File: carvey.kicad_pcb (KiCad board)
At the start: 2 copper layers, 48.2 x 14.7 mm, 2 parts, among them J1 Conn_01x04, SW1 SW_Push_Dual

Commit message: Added holes, carved it with Carvey itself, without autoleveling
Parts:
- added REF**: M2.5_HOLE, adamgreig/agg-kicad/agg.pretty:M2.5_HOLE, F.Cu at (140.8, 100.2)
- added REF**: M2.5_HOLE, adamgreig/agg-kicad/agg.pretty:M2.5_HOLE, F.Cu at (130.9, 100.2)
- added REF**: M2.5_HOLE, adamgreig/agg-kicad/agg.pretty:M2.5_HOLE, F.Cu at (140.8, 90.5)
- added REF**: M2.5_HOLE, adamgreig/agg-kicad/agg.pretty:M2.5_HOLE, F.Cu at (130.9, 90.4)
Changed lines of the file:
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@@
   (tracks 16)
   (zones 0)
-  (modules 2)
+  (modules 6)
   (nets 3)
 )
@@
   (tracks 16)
   (zones 0)
-  (modules 2)
+  (modules 6)
   (nets 3)
 )
@@
 )
 (setup
-  (last_trace_width 1)
+  (last_trace_width 0.25)
   (user_trace_width 1)
   (user_trace_width 2)
@@
   (mod_text_size 1 1)
   (mod_text_width 0.15)
-  (pad_size 1.524 1.524)
-  (pad_drill 0.762)
+  (pad_size 2 2)
+  (pad_drill 2)
   (pad_to_mask_clearance 0.2)
   (aux_axis_origin 127.05 102.65)
@@
     (viasonmask false)
     (mode 1)
-    (useauxorigin false)
+    (useauxorigin true)
     (hpglpennumber 1)
     (hpglpenspeed 20)
@@
     (drillshape 0)
     (scaleselection 1)
-    (outputdirectory homefab))
+    (outputdirectory homefab/))
 )
 (net 0 "")
@@
   (add_net "Net-(J1-Pad2)")
 )
+  (module adamgreig/agg-kicad/agg.pretty:M2.5_HOLE (layer F.Cu)
+    (at 140.85 100.2)
+    (fp_text reference REF** (at 0 -2.5) (layer F.Fab) hide
+      (effects (font (size 1 1) (thickness 0.15)))
+    )
+    (fp_text value M2.5_HOLE (at 0 2.5) (layer F.Fab) hide
+      (effects (font (size 1 1) (thickness 0.15)))
+    )
+    (fp_line (start -1.8 -1.8) (end 1.8 -1.8) (layer F.CrtYd) (width 0.01))
+    (fp_line (start 1.8 -1.8) (end 1.8 1.8) (layer F.CrtYd) (width 0.01))
+    (fp_line (start 1.8 1.8) (end -1.8 1.8) (layer F.CrtYd) (width 0.01))
+    (fp_line (start -1.8 1.8) (end -1.8 -1.8) (layer F.CrtYd) (width 0.01))
+    (pad "" np_thru_hole circle (at 0 0) (size 2 2) (drill 2) (layers *.Cu F.Mask))
+  )
+  (module adamgreig/agg-kicad/agg.pretty:M2.5_HOLE (layer F.Cu)
+    (at 130.9 100.2)
+    (fp_text reference REF** (at 0 -2.5) (layer F.Fab) hide
+      (effects (font (size 1 1) (thickness 0.15)))
+    )
+    (fp_text value M2.5_HOLE (at 0 2.5) (layer F.Fab) hide
+      (effects (font (size 1 1) (thickness 0.15)))
+    )
+    (fp_line (start -1.8 -1.8) (end 1.8 -1.8) (layer F.CrtYd) (width 0.01))
+    (fp_line (start 1.8 -1.8) (end 1.8 1.8) (layer F.CrtYd) (width 0.01))
+    (fp_line (start 1.8 1.8) (end -1.8 1.8) (layer F.CrtYd) (width 0.01))
+    (fp_line (start -1.8 1.8) (end -1.8 -1.8) (layer F.CrtYd) (width 0.01))
+    (pad "" np_thru_hole circle (at 0 0) (size 2 2) (drill 2) (layers *.Cu F.Mask))
+  )
+  (module adamgreig/agg-kicad/agg.pretty:M2.5_HOLE (layer F.Cu)
+    (at 140.85 90.45)
+    (fp_text reference REF** (at 0 -2.5) (layer F.Fab) hide
+      (effects (font (size 1 1) (thickness 0.15)))
+    )
+    (fp_text value M2.5_HOLE (at 0 2.5) (layer F.Fab) hide
+      (effects (font (size 1 1) (thickness 0.15)))
+    )
+    (fp_line (start -1.8 -1.8) (end 1.8 -1.8) (layer F.CrtYd) (width 0.01))
+    (fp_line (start 1.8 -1.8) (end 1.8 1.8) (layer F.CrtYd) (width 0.01))
+    (fp_line (start 1.8 1.8) (end -1.8 1.8) (layer F.CrtYd) (width 0.01))
+    (fp_line (start -1.8 1.8) (end -1.8 -1.8) (layer F.CrtYd) (width 0.01))
+    (pad "" np_thru_hole circle (at 0 0) (size 2 2) (drill 2) (layers *.Cu F.Mask))
+  )
+  (module adamgreig/agg-kicad/agg.pretty:M2.5_HOLE (layer F.Cu)
+    (at 130.925 90.4)
+    (fp_text reference REF** (at 0 -2.5) (layer F.Fab) hide
+      (effects (font (size 1 1) (thickness 0.15)))
+    )
+    (fp_text value M2.5_HOLE (at 0 2.5) (layer F.Fab) hide
+      (effects (font (size 1 1) (thickness 0.15)))
+    )
+    (fp_line (start -1.8 -1.8) (end 1.8 -1.8) (layer F.CrtYd) (width 0.01))
+    (fp_line (start 1.8 -1.8) (end 1.8 1.8) (layer F.CrtYd) (width 0.01))
+    (fp_line (start 1.8 1.8) (end -1.8 1.8) (layer F.CrtYd) (width 0.01))
+    (fp_line (start -1.8 1.8) (end -1.8 -1.8) (layer F.CrtYd) (width 0.01))
+    (pad "" np_thru_hole circle (at 0 0) (size 2 2) (drill 2) (layers *.Cu F.Mask))
+  )
   (module KiCad/Connectors_JST.pretty:JST_PH_S4B-PH-SM4-TB_04x2.00mm_Angled (layer F.Cu)
     (at 153.5 95.025 90)

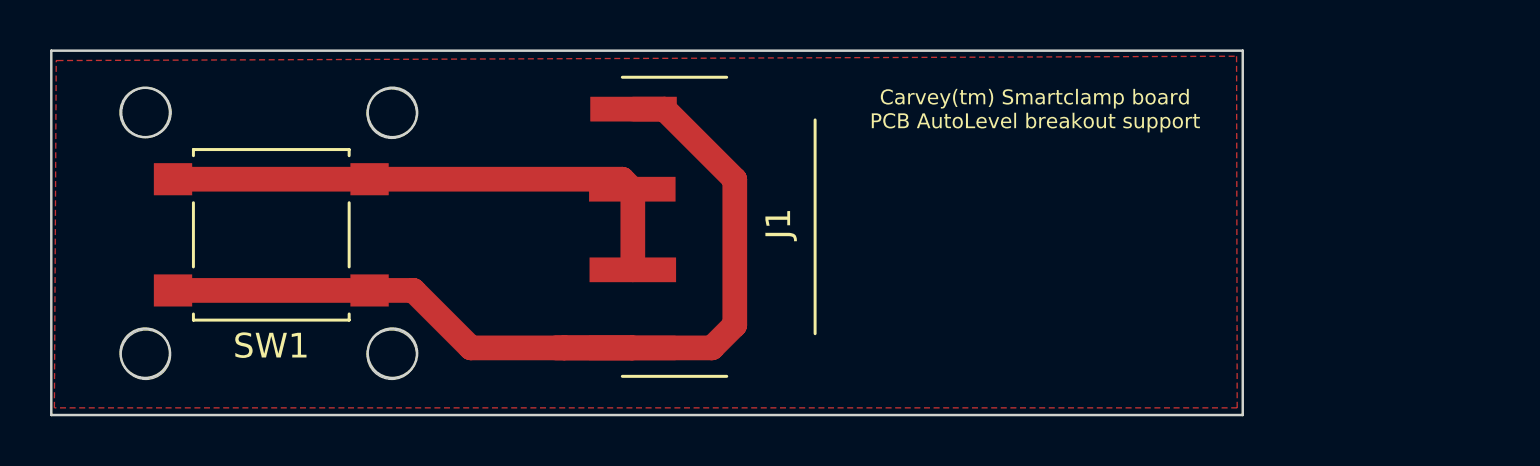
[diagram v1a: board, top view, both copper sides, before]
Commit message: Track too near pad
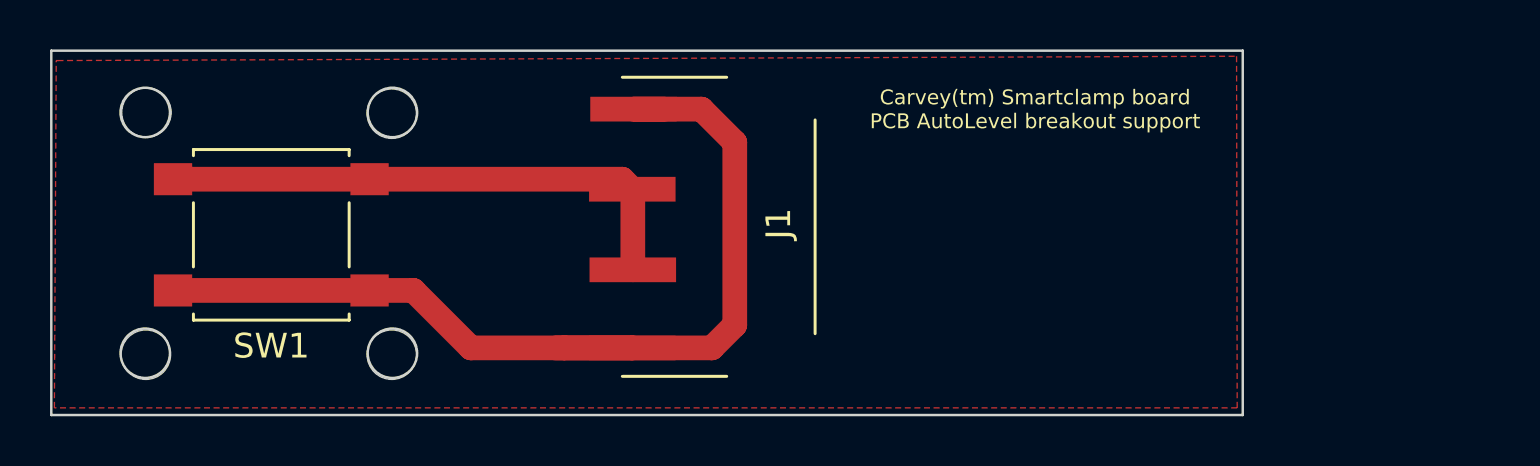
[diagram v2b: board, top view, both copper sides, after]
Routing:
- net Net-(J1-Pad1): track 38.3 -> 40.5 mm
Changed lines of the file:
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@@
   (thickness 1.6)
   (drawings 10)
-  (tracks 16)
+  (tracks 17)
   (zones 0)
   (modules 6)
@@
   (thickness 1.6)
   (drawings 10)
-  (tracks 16)
+  (tracks 17)
   (zones 0)
   (modules 6)
@@
 )
 (setup
-  (last_trace_width 0.25)
+  (last_trace_width 1)
   (user_trace_width 1)
   (user_trace_width 2)
@@
   (gr_line (start 175.275 87.9) (end 175.275 102.64) (layer Edge.Cuts) (width 0.1))
   (gr_circle (center 130.875 90.4) (end 131.875 90.4) (layer Edge.Cuts) (width 0.1))
+  (segment (start 150.63 90.265) (end 153.38 90.265) (width 1) (layer F.Cu) (net 1))
+  (segment (start 153.38 90.265) (end 154.725 91.61) (width 1) (layer F.Cu) (net 1))
+  (segment (start 154.725 91.61) (end 154.725 99) (width 1) (layer F.Cu) (net 1))
+  (segment (start 154.725 99) (end 153.8 99.925) (width 1) (layer F.Cu) (net 1))
+  (segment (start 153.8 99.925) (end 150.58 99.925) (width 1) (layer F.Cu) (net 1))
   (segment (start 132 97.6) (end 139.95 97.6) (width 1) (layer F.Cu) (net 1))
   (segment (start 139.95 97.6) (end 141.725 97.6) (width 1) (layer F.Cu) (net 1))
@@
   (segment (start 147.83 99.925) (end 150.58 99.925) (width 1) (layer F.Cu) (net 1))
   (segment (start 147.475 99.925) (end 150.58 99.925) (width 1) (layer F.Cu) (net 1))
-  (segment (start 154.725 99) (end 153.8 99.925) (width 1) (layer F.Cu) (net 1))
-  (segment (start 153.8 99.925) (end 150.58 99.925) (width 1) (layer F.Cu) (net 1))
-  (segment (start 154.725 93.11) (end 154.725 99) (width 1) (layer F.Cu) (net 1))
   (segment (start 150.63 90.265) (end 151.88 90.265) (width 1) (layer F.Cu) (net 1))
-  (segment (start 151.88 90.265) (end 154.725 93.11) (width 1) (layer F.Cu) (net 1))
   (segment (start 139.95 93.1) (end 150.175 93.1) (width 1) (layer F.Cu) (net 2))
   (segment (start 150.175 93.1) (end 150.58 93.505) (width 1) (layer F.Cu) (net 2))

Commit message: Add new board outline with external overhang for alligator clips, need to add the pads
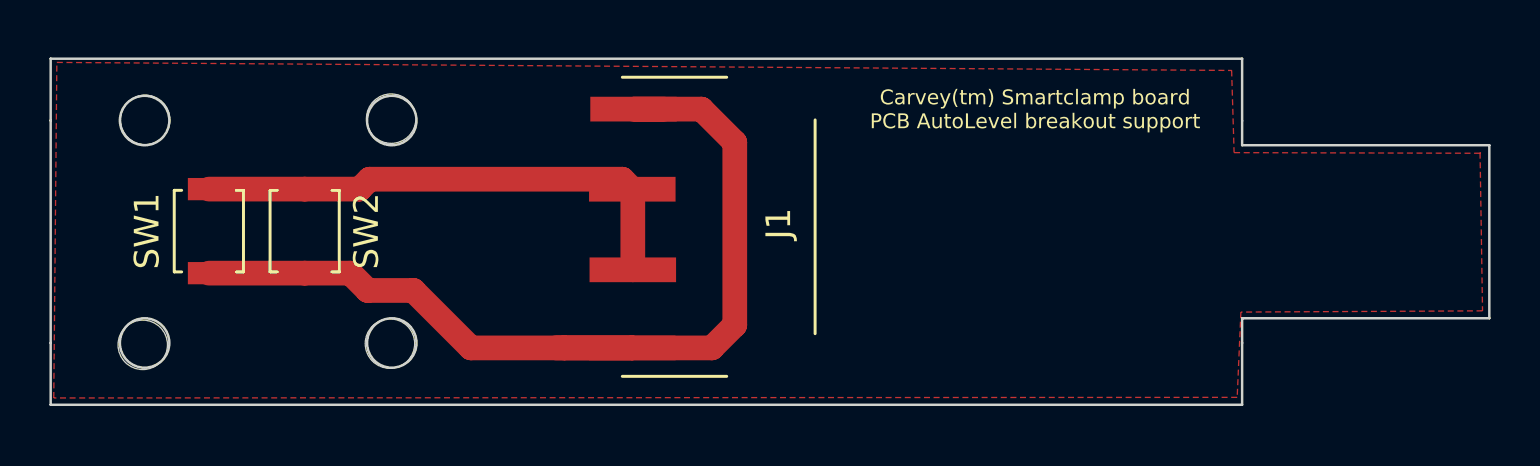
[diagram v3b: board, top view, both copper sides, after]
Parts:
- added SW2: SW_Push, KiCad/Buttons_Switches_SMD.pretty:SW_SPST_B3U-1000P, F.Cu at (137.3, 95.2)
- SW1: value SW_Push_Dual -> SW_Push; footprint KiCad/Buttons_Switches_SMD.pretty:SW_SPST_B3S-1000 -> KiCad/Buttons_Switches_SMD.pretty:SW_SPST_B3U-1000P
- moved SW1 2.53 mm to (133.4, 95.2), turned to 90 degrees
- moved REF** 0.46 mm to (140.8, 99.8)
- moved REF** 0.42 mm to (130.8, 99.8)
- moved REF** 0.30 mm to (130.9, 90.7)
- moved REF** 0.20 mm to (140.8, 90.7)
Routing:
- net Net-(J1-Pad2): track 22.0 -> 20.7 mm
- net Net-(J1-Pad1): track 40.5 -> 39.3 mm
- added copper zone on F.Cu, net Net-(J1-Pad1)
- removed copper zone on F.Cu, net (none)
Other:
- board size 48.2 x 14.7 mm -> 58.2 x 14 mm

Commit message: New version of the board with protruding pads for the alligator clips
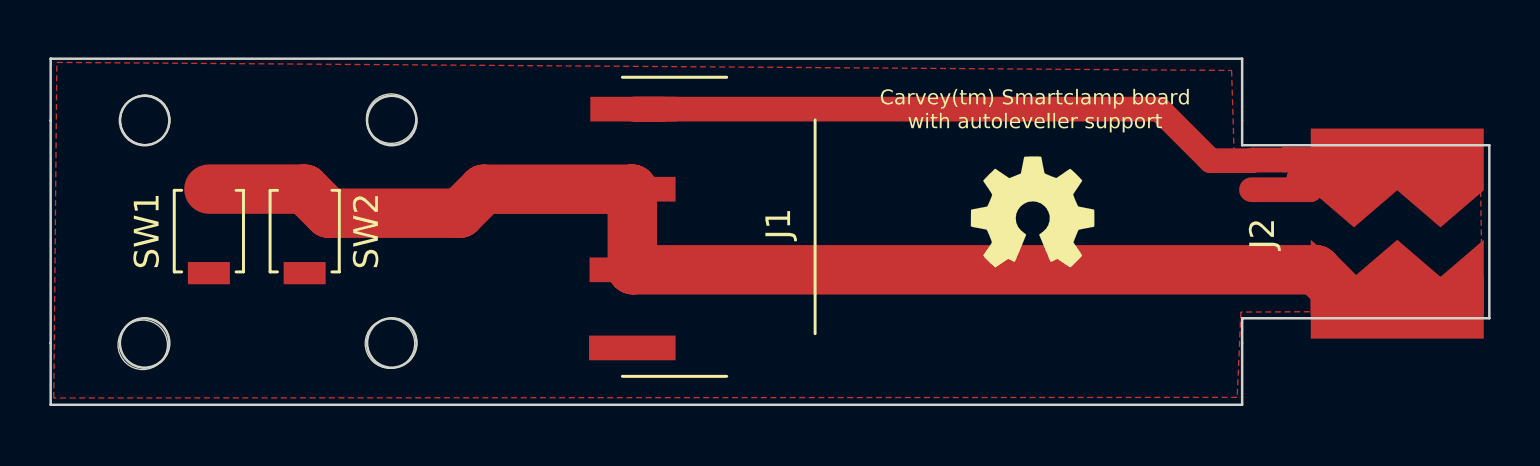
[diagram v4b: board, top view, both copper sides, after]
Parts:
- added J2: Conn_01x02, alligator_pads:TouchSlider-2_10x7mm, F.Cu at (181.5, 95.3)
- added LOGO_OSHW_silkscreen_5mm: val**, freetronics/freetronics_kicad_library/freetronics_footprints.pretty:LOGO_OSHW_silkscreen_5mm, F.Cu at (166.8, 94.4)
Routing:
- net Net-(J1-Pad2): track 20.7 -> 54.2 mm
- net Net-(J1-Pad1): track 39.3 -> 46.0 mm
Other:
- net class Default: clearance 0.2 -> 0.5; trace_width 0.25 -> 0.5
- rule trace_clearance: 0.2 -> 0.5
- board text added: "Carvey(tm) Smartclamp board with autoleveller support"
- board text removed: "Carvey(tm) Smartclamp board PCB AutoLevel breakout support"
